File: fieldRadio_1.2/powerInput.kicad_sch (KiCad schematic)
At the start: 7 parts, among them Q21 IRF9540, U10 LM1086-5.0

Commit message: Working on fieldRadio_1.2 schematics
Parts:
- added C230, C231: 4.7uF, PCM_JLCPCB:C_0805, symbol PCM_JLCPCB-Capacitors:0805,4.7uF
- added C232, C233: 100nF, PCM_JLCPCB:C_0603, symbol PCM_JLCPCB-Capacitors:0603,100nF
- added C234, C235: 22uF, PCM_JLCPCB:C_0805, symbol PCM_JLCPCB-Capacitors:0805,22uF
- added C236: 100uF, Capacitor_SMD:C_Elec_6.3x5.8, symbol Device:C_Small_US
- added J13, J9: Conn_01x03, Connector_Wire:SolderWire-0.75sqmm_1x03_P4.8mm_D1.25mm_OD2.3mm, symbol Connector_Generic:Conn_01x03
- added L22: 6.8uH, Inductor_SMD:L_TechFuse_SL0624, symbol Device:L
- added R208: 10kΩ, PCM_JLCPCB:R_0603, symbol PCM_JLCPCB-Resistors:0603,10kΩ
- added R214: 14kΩ, PCM_JLCPCB:R_0603, symbol PCM_JLCPCB-Resistors:0603,30kΩ
- added R220: 100k, PCM_JLCPCB:R_0603, symbol PCM_JLCPCB-Resistors:0603,10kΩ
- added U29: LMR51430, Package_TO_SOT_SMD:SOT-23-6, symbol Regulator_Switching:LMR51430
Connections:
- net +5V: now also J9.2 (Pin_2); no longer C155.1, C156.1, U10.2 (VO)
- net GND: now also C230.2, C231.2, C232.2, C234.2, C235.2, C236.2, R208.2, R214.2, U29.1 (GND)
- net VDD12: now also J13.2 (Pin_2); no longer C153.1, C154.1, U10.3 (VI)
- net at Q21.2 (D): no longer F1.2
- new net: C230.1, C231.1, C232.1, J13.1 (Pin_1), R208.1, U29.3 (VIN), U29.5 (EN)
- new net: C153.1, C154.1, J13.3 (Pin_3), U10.3 (VI)
- new net: C233.1, U29.6 (CB)
- new net +5V_Linear: C155.1, C156.1, J9.3 (Pin_3), U10.2 (VO)
- new net +5V_SWITCHING: C234.1, C235.1, C236.1, J9.1 (Pin_1), L22.2, R220.2
- new net fb2: R214.1, R220.1, U29.4 (FB)
- new net sw2: C233.2, L22.1, U29.2 (SW)
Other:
- moved on the sheet: F1, Q21

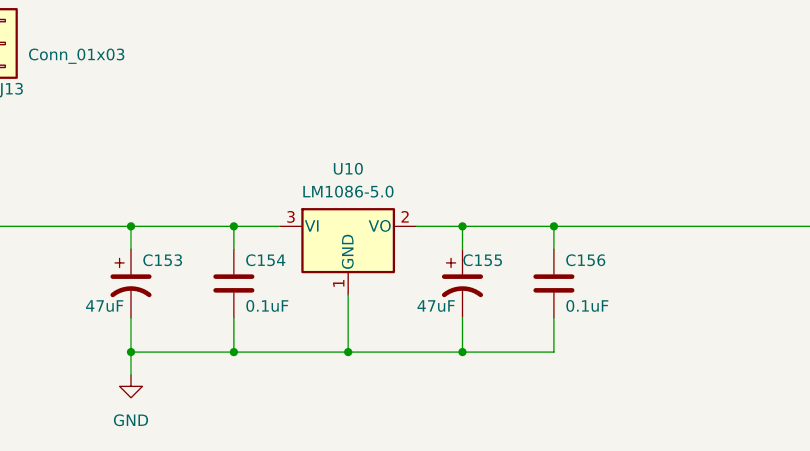
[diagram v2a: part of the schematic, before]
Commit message: adding jlcpcb part numbers to schematics
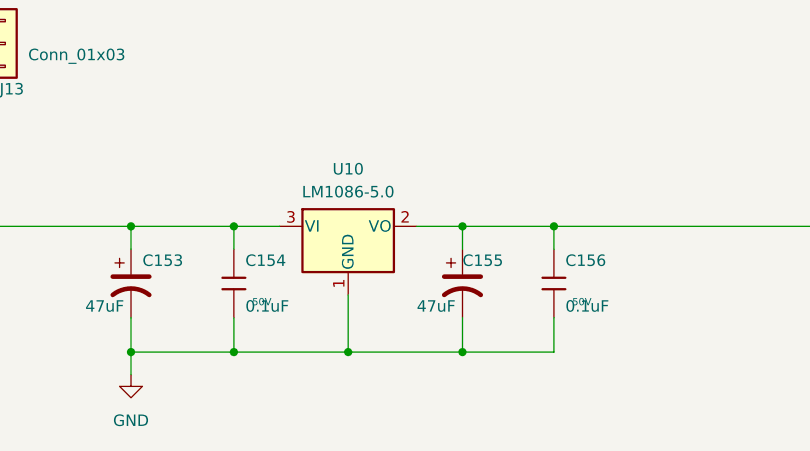
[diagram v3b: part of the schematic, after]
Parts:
- C154, C156: footprint Capacitor_SMD:C_0603_1608Metric_Pad1.08x0.95mm_HandSolder -> PCM_JLCPCB:C_0603; symbol Device:C -> PCM_JLCPCB-Capacitors:0603,100nF; Attrition Qty (none) -> 10; Capacitance (none) -> 100nF; Category (none) -> Capacitors,Multilayer Ceramic Capacitors MLCC - SMD/SMT; Class (none) -> Basic Component; LCSC (none) -> C14663; Manufacturer (none) -> YAGEO; Minimum Qty (none) -> 20; Part (none) -> CC0603KRX7R9BB104; Price (none) -> 0.006USD; Process (none) -> SMT; Stock (none) -> 70324515; Temperature Coefficient (none) -> X7R; Tolerance (none) -> ±10%; Voltage Rated (none) -> 50V
- R220: symbol PCM_JLCPCB-Resistors:0603,10kΩ -> PCM_JLCPCB-Resistors:0603,100kΩ; LCSC C25804 -> C25803; Part 0603WAF1002T5E -> 0603WAF1003T5E; Resistance 10kΩ -> 100kΩ; Stock 51181774 -> 7820113

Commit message: more jlcpcb part number work
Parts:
- F1: JLCPCB (none) -> C139284
- Q21: JLCPCB (none) -> C2575; now left out of the parts list
- U10: JLCPCB (none) -> C16807
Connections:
- net at Q21.2 (D): now also F1.2
- net fb2: no longer names the net of R214.1, R220.1, U29.4 (FB)
- net sw2: no longer names the net of C233.2, L22.1, U29.2 (SW)
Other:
- moved on the sheet: F1
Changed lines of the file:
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@@
 	(wire
 		(pts
-			(xy 97.028 125.73) (xy 107.95 125.73)
-		)
-		(stroke
-			(width 0)
-			(type default)
-		)
-	)
-	(wire
-		(pts
 			(xy 223.52 110.49) (xy 232.41 110.49)
 		)
@@
 	(wire
 		(pts
-			(xy 86.36 125.73) (xy 89.154 125.73)
+			(xy 86.36 125.73) (xy 90.17 125.73)
+		)
+		(stroke
+			(width 0)
+			(type default)
+		)
+	)
+	(wire
+		(pts
+			(xy 97.79 125.73) (xy 107.95 125.73)
 		)
 		(stroke
@@
 		)
 	)
-	(label "sw2"
-		(at 267.97 92.71 0)
-		(effects
-			(font
-				(size 1.27 1.27)
-			)
-			(justify left bottom)
-		)
-	)
 	(label "+5V_SWITCHING"
 		(at 317.5 92.71 0)
@@
 		)
 	)
-	(label "fb2"
-		(at 273.05 95.25 0)
-		(effects
-			(font
-				(size 1.27 1.27)
-			)
-			(justify left bottom)
-		)
-	)
 	(global_label "VDD12"
 		(shape input)
@@
 			)
 		)
+		(property "Mouser Part Number" ""
+			(at 232.41 139.7 0)
+			(hide yes)
+			(show_name no)
+			(do_not_autoplace no)
+			(effects
+				(font
+					(size 1.27 1.27)
+				)
+			)
+		)
+		(property "JLCPCB" "C16807"
+			(at 232.41 139.7 0)
+			(hide yes)
+			(show_name no)
+			(do_not_autoplace no)
+			(effects
+				(font
+					(size 1.27 1.27)
+				)
+			)
+		)
 		(pin "1"
 		)
@@
 		(body_style 1)
 		(exclude_from_sim no)
-		(in_bom yes)
+		(in_bom no)
 		(on_board yes)
 		(in_pos_files yes)
@@
 			)
 		)
+		(property "Mouser Part Number" ""
+			(at 113.03 128.27 0)
+			(hide yes)
+			(show_name no)
+			(do_not_autoplace no)
+			(effects
+				(font
+					(size 1.27 1.27)
+				)
+			)
+		)
+		(property "JLCPCB" "C2575"
+			(at 113.03 128.27 90)
+			(hide yes)
+			(show_name no)
+			(do_not_autoplace no)
+			(effects
+				(font
+					(size 1.27 1.27)
+				)
+			)
+		)
 		(pin "1"
 		)
@@
 	(symbol
 		(lib_id "Device:Fuse")
-		(at 92.964 125.73 90)
+		(at 93.98 125.73 90)
 		(unit 1)
 		(body_style 1)
@@
 		(fields_autoplaced yes)
 		(property "Reference" "F1"
-			(at 92.964 119.38 90)
+			(at 93.98 119.38 90)
 			(show_name no)
 			(do_not_autoplace no)
@@
 		)
 		(property "Value" "Polyfuse"
-			(at 92.964 121.92 90)
+			(at 93.98 121.92 90)
 			(show_name no)
 			(do_not_autoplace no)
@@
 		)
 		(property "Footprint" "Fuse:Fuse_2920_7451Metric_Pad2.10x5.45mm_HandSolder"
-			(at 92.964 127.508 90)
+			(at 93.98 127.508 90)
 			(hide yes)
 			(show_name no)
@@
 		)
 		(property "Datasheet" ""
-			(at 92.964 125.73 0)
+			(at 93.98 125.73 0)
 			(hide yes)
 			(show_name no)
@@
 		)
 		(property "Description" ""
-			(at 92.964 125.73 0)
+			(at 93.98 125.73 0)
+			(show_name no)
+			(do_not_autoplace no)
+			(effects
+				(font
+					(size 1.27 1.27)
+				)
+			)
+		)
+		(property "Mouser Part Number" ""
+			(at 93.98 125.73 0)
+			(hide yes)
+			(show_name no)
+			(do_not_autoplace no)
+			(effects
+				(font
+					(size 1.27 1.27)
+				)
+			)
+		)
+		(property "JLCPCB" "C139284"
+			(at 93.98 125.73 90)
+			(hide yes)
 			(show_name no)
 			(do_not_autoplace no)

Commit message: continued symbol property updates
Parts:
- removed C153, C155: 47uF, Capacitor_THT:CP_Radial_D7.5mm_P2.50mm, symbol Device:C_Polarized_US
- removed R214: 14kΩ, PCM_JLCPCB:R_0603, symbol PCM_JLCPCB-Resistors:0603,30kΩ
- added C54, C55: 47uF, Capacitor_SMD:CP_Elec_6.3x5.8, symbol Device:C_Polarized_US
- added R224: 12kΩ, PCM_JLCPCB:R_0603, symbol PCM_JLCPCB-Resistors:0603,12kΩ
- added R225: 2kΩ, PCM_JLCPCB:R_0603, symbol PCM_JLCPCB-Resistors:0603,2kΩ
- F1: LCSC (none) -> C139284
- J13, J9: now left out of the parts list
- L22: LCSC (none) -> C22463814
- Q21: LCSC (none) -> C2575
- U10: LCSC (none) -> C16807; now left out of the parts list
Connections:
- net +5V_Linear: now also C55.1
- net GND: now also C54.2, C55.2, R225.2
- net at C154.1, J13.3 (Pin_3), U10.3 (VI): now also C54.1
- net at R220.1, U29.4 (FB): now also R224.2
- new net: R224.1, R225.1

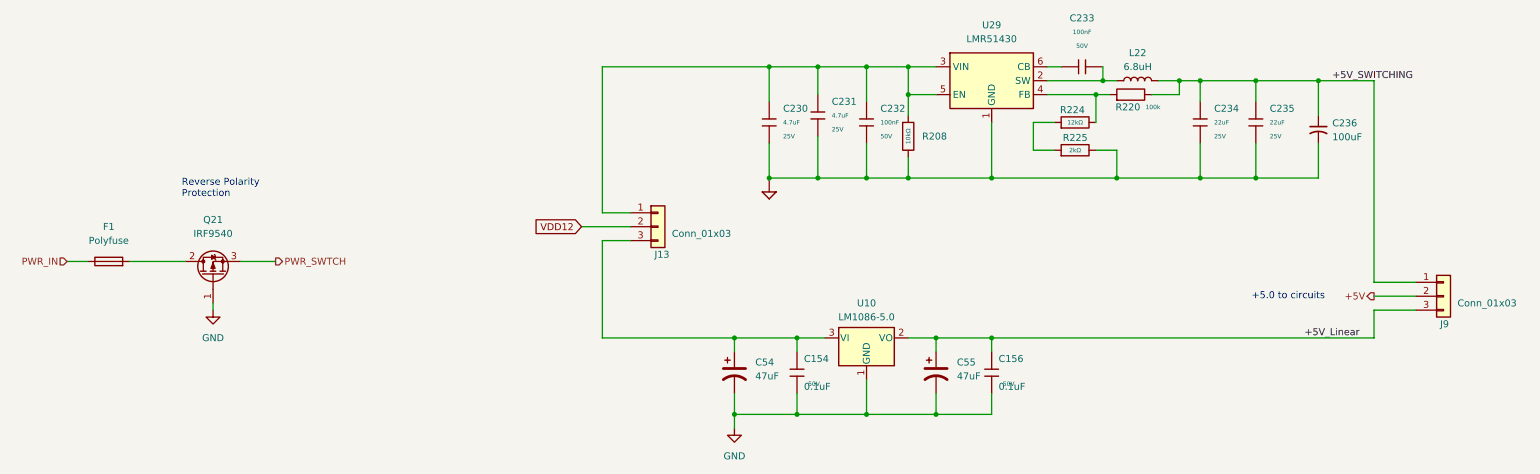
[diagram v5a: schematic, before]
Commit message: Starting fieldRadio1.2 layout
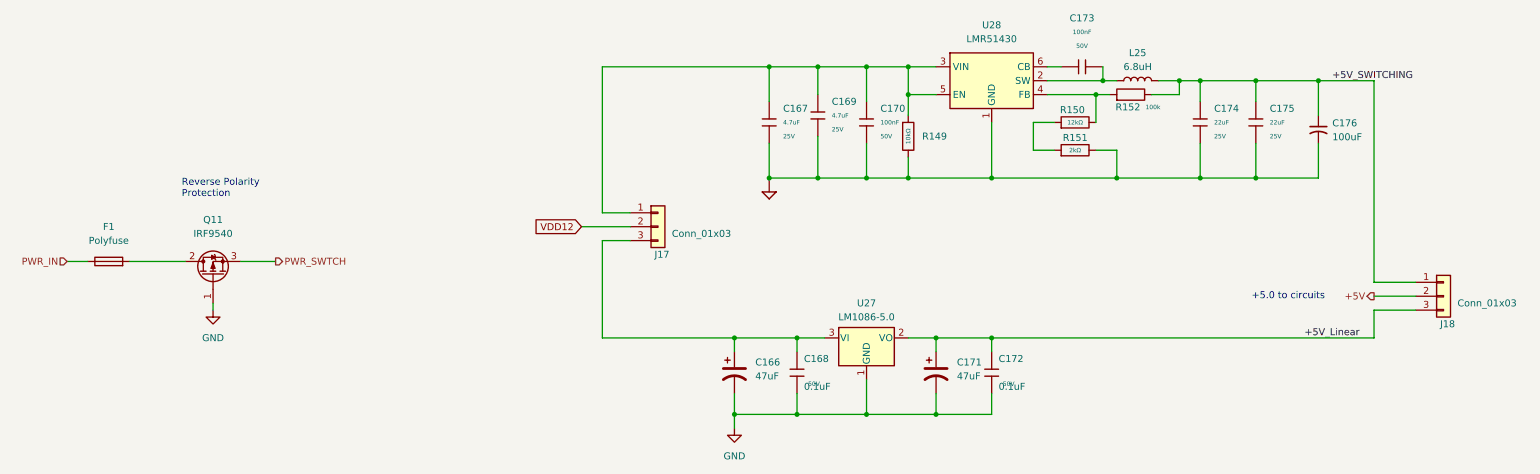
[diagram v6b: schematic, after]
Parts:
- renumbered C54 to C166, C230 to C167, C154 to C168, C231 to C169, C232 to C170, C55 to C171, C156 to C172, C233 to C173, C234 to C174, C235 to C175, C236 to C176, J13 to J17, J9 to J18, L22 to L25, Q21 to Q11, R208 to R149, R224 to R150, R225 to R151, R220 to R152, U10 to U27, U29 to U28
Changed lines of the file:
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@@
 		(in_pos_files yes)
 		(dnp no)
-		(property "Reference" "J13"
+		(property "Reference" "J17"
 			(at 193.675 124.46 0)
 			(show_name no)
@@
 			(project "fieldRadio_1.2"
 				(path "/a1d1b2b0-2f27-4dc0-94ba-bb0e02933617/56bfcbb6-5b4c-41a3-a0f1-0c3e063460f4"
-					(reference "J13")
+					(reference "J17")
 					(unit 1)
 				)
@@
 		(dnp no)
 		(fields_autoplaced yes)
-		(property "Reference" "C55"
+		(property "Reference" "C171"
 			(at 248.92 144.1449 0)
 			(show_name no)
@@
 			(project "fieldRadio_1.2"
 				(path "/a1d1b2b0-2f27-4dc0-94ba-bb0e02933617/56bfcbb6-5b4c-41a3-a0f1-0c3e063460f4"
-					(reference "C55")
+					(reference "C171")
 					(unit 1)
 				)
@@
 		(in_pos_files yes)
 		(dnp no)
-		(property "Reference" "#SUPPLY042"
+		(property "Reference" "#SUPPLY030"
 			(at 214.63 113.03 0)
 			(hide yes)
@@
 			(project "fieldRadio_1.2"
 				(path "/a1d1b2b0-2f27-4dc0-94ba-bb0e02933617/56bfcbb6-5b4c-41a3-a0f1-0c3e063460f4"
-					(reference "#SUPPLY042")
+					(reference "#SUPPLY030")
 					(unit 1)
 				)
@@
 		(dnp no)
 		(fields_autoplaced yes)
-		(property "Reference" "C54"
+		(property "Reference" "C166"
 			(at 212.09 144.1449 0)
 			(show_name no)
@@
 			(project "fieldRadio_1.2"
 				(path "/a1d1b2b0-2f27-4dc0-94ba-bb0e02933617/56bfcbb6-5b4c-41a3-a0f1-0c3e063460f4"
-					(reference "C54")
+					(reference "C166")
 					(unit 1)
 				)
@@
 		(in_pos_files yes)
 		(dnp no)
-		(property "Reference" "C154"
+		(property "Reference" "C168"
 			(at 220.98 143.51 0)
 			(show_name no)
@@
 			(project "fieldRadio_1.2"
 				(path "/a1d1b2b0-2f27-4dc0-94ba-bb0e02933617/56bfcbb6-5b4c-41a3-a0f1-0c3e063460f4"
-					(reference "C154")
+					(reference "C168")
 					(unit 1)
 				)
@@
 		(in_pos_files yes)
 		(dnp no)
-		(property "Reference" "R225"
+		(property "Reference" "R151"
 			(at 272.796 103.124 90)
 			(show_name no)
@@
 			(project "fieldRadio_1.2"
 				(path "/a1d1b2b0-2f27-4dc0-94ba-bb0e02933617/56bfcbb6-5b4c-41a3-a0f1-0c3e063460f4"
-					(reference "R225")
+					(reference "R151")
 					(unit 1)
 				)
@@
 		(dnp no)
 		(fields_autoplaced yes)
-		(property "Reference" "C231"
+		(property "Reference" "C169"
 			(at 226.06 96.5199 0)
 			(show_name no)
@@
 			(project "fieldRadio_1.2"
 				(path "/a1d1b2b0-2f27-4dc0-94ba-bb0e02933617/56bfcbb6-5b4c-41a3-a0f1-0c3e063460f4"
-					(reference "C231")
+					(reference "C169")
 					(unit 1)
 				)
@@
 		(in_pos_files yes)
 		(dnp no)
-		(property "Reference" "R220"
+		(property "Reference" "R152"
 			(at 280.162 97.536 90)
 			(show_name no)
@@
 			(project "fieldRadio_1.2"
 				(path "/a1d1b2b0-2f27-4dc0-94ba-bb0e02933617/56bfcbb6-5b4c-41a3-a0f1-0c3e063460f4"
-					(reference "R220")
+					(reference "R152")
 					(unit 1)
 				)
@@
 		(dnp no)
 		(fields_autoplaced yes)
-		(property "Reference" "U10"
+		(property "Reference" "U27"
 			(at 232.41 133.35 0)
 			(show_name no)
@@
 			(project "fieldRadio_1.2"
 				(path "/a1d1b2b0-2f27-4dc0-94ba-bb0e02933617/56bfcbb6-5b4c-41a3-a0f1-0c3e063460f4"
-					(reference "U10")
+					(reference "U27")
 					(unit 1)
 				)
@@
 		(dnp no)
 		(fields_autoplaced yes)
-		(property "Reference" "C233"
+		(property "Reference" "C173"
 			(at 271.78 81.28 90)
 			(show_name no)
@@
 			(project "fieldRadio_1.2"
 				(path "/a1d1b2b0-2f27-4dc0-94ba-bb0e02933617/56bfcbb6-5b4c-41a3-a0f1-0c3e063460f4"
-					(reference "C233")
+					(reference "C173")
 					(unit 1)
 				)
@@
 		(dnp no)
 		(fields_autoplaced yes)
-		(property "Reference" "Q21"
+		(property "Reference" "Q11"
 			(at 113.03 118.11 90)
 			(show_name no)
@@
 			(project "fieldRadio_1.2"
 				(path "/a1d1b2b0-2f27-4dc0-94ba-bb0e02933617/56bfcbb6-5b4c-41a3-a0f1-0c3e063460f4"
-					(reference "Q21")
+					(reference "Q11")
 					(unit 1)
 				)
@@
 		(dnp no)
 		(fields_autoplaced yes)
-		(property "Reference" "C232"
+		(property "Reference" "C170"
 			(at 234.95 97.7899 0)
 			(show_name no)
@@
 			(project "fieldRadio_1.2"
 				(path "/a1d1b2b0-2f27-4dc0-94ba-bb0e02933617/56bfcbb6-5b4c-41a3-a0f1-0c3e063460f4"
-					(reference "C232")
+					(reference "C170")
 					(unit 1)
 				)
@@
 		(dnp no)
 		(fields_autoplaced yes)
-		(property "Reference" "C236"
+		(property "Reference" "C176"
 			(at 317.5 100.4569 0)
 			(show_name no)
@@
 			(project "fieldRadio_1.2"
 				(path "/a1d1b2b0-2f27-4dc0-94ba-bb0e02933617/56bfcbb6-5b4c-41a3-a0f1-0c3e063460f4"
-					(reference "C236")
+					(reference "C176")
 					(unit 1)
 				)
@@
 		(dnp no)
 		(fields_autoplaced yes)
-		(property "Reference" "#PWR029"
+		(property "Reference" "#PWR052"
 			(at 113.03 140.97 0)
 			(hide yes)
@@
 			(project "fieldRadio_1.2"
 				(path "/a1d1b2b0-2f27-4dc0-94ba-bb0e02933617/56bfcbb6-5b4c-41a3-a0f1-0c3e063460f4"
-					(reference "#PWR029")
+					(reference "#PWR052")
 					(unit 1)
 				)
@@
 		(in_pos_files yes)
 		(dnp no)
-		(property "Reference" "C156"
+		(property "Reference" "C172"
 			(at 256.54 143.51 0)
 			(show_name no)
@@
 			(project "fieldRadio_1.2"
 				(path "/a1d1b2b0-2f27-4dc0-94ba-bb0e02933617/56bfcbb6-5b4c-41a3-a0f1-0c3e063460f4"
-					(reference "C156")
+					(reference "C172")
 					(unit 1)
 				)
@@
 		(in_pos_files yes)
 		(dnp no)
-		(property "Reference" "R224"
+		(property "Reference" "R150"
 			(at 272.288 98.044 90)
 			(show_name no)
@@
 			(project "fieldRadio_1.2"
 				(path "/a1d1b2b0-2f27-4dc0-94ba-bb0e02933617/56bfcbb6-5b4c-41a3-a0f1-0c3e063460f4"
-					(reference "R224")
+					(reference "R150")
 					(unit 1)
 				)
@@
 		(dnp no)
 		(fields_autoplaced yes)
-		(property "Reference" "R208"
+		(property "Reference" "R149"
 			(at 242.57 102.8699 0)
 			(show_name no)
@@
 			(project "fieldRadio_1.2"
 				(path "/a1d1b2b0-2f27-4dc0-94ba-bb0e02933617/56bfcbb6-5b4c-41a3-a0f1-0c3e063460f4"
-					(reference "R208")
+					(reference "R149")
 					(unit 1)
 				)
@@
 		(dnp no)
 		(fields_autoplaced yes)
-		(property "Reference" "U29"
+		(property "Reference" "U28"
 			(at 255.27 82.55 0)
 			(show_name no)
@@
 			(project "fieldRadio_1.2"
 				(path "/a1d1b2b0-2f27-4dc0-94ba-bb0e02933617/56bfcbb6-5b4c-41a3-a0f1-0c3e063460f4"
-					(reference "U29")
+					(reference "U28")
 					(unit 1)
 				)
@@
 		(dnp no)
 		(fields_autoplaced yes)
-		(property "Reference" "C230"
+		(property "Reference" "C167"
 			(at 217.17 97.7899 0)
 			(show_name no)
@@
 			(project "fieldRadio_1.2"
 				(path "/a1d1b2b0-2f27-4dc0-94ba-bb0e02933617/56bfcbb6-5b4c-41a3-a0f1-0c3e063460f4"
-					(reference "C230")
+					(reference "C167")
 					(unit 1)
 				)
@@
 		(dnp no)
 		(fields_autoplaced yes)
-		(property "Reference" "C235"
+		(property "Reference" "C175"
 			(at 306.07 97.7899 0)
 			(show_name no)
@@
 			(project "fieldRadio_1.2"
 				(path "/a1d1b2b0-2f27-4dc0-94ba-bb0e02933617/56bfcbb6-5b4c-41a3-a0f1-0c3e063460f4"
-					(reference "C235")
+					(reference "C175")
 					(unit 1)
 				)
@@
 		(dnp no)
 		(fields_autoplaced yes)
-		(property "Reference" "L22"
+		(property "Reference" "L25"
 			(at 281.94 87.63 90)
 			(show_name no)
@@
 			(project "fieldRadio_1.2"
 				(path "/a1d1b2b0-2f27-4dc0-94ba-bb0e02933617/56bfcbb6-5b4c-41a3-a0f1-0c3e063460f4"
-					(reference "L22")
+					(reference "L25")
 					(unit 1)
 				)
@@
 		(dnp no)
 		(fields_autoplaced yes)
-		(property "Reference" "C234"
+		(property "Reference" "C174"
 			(at 295.91 97.7899 0)
 			(show_name no)
@@
 			(project "fieldRadio_1.2"
 				(path "/a1d1b2b0-2f27-4dc0-94ba-bb0e02933617/56bfcbb6-5b4c-41a3-a0f1-0c3e063460f4"
-					(reference "C234")
+					(reference "C174")
 					(unit 1)
 				)
@@
 		(dnp no)
 		(fields_autoplaced yes)
-		(property "Reference" "#PWR039"
+		(property "Reference" "#PWR053"
 			(at 208.28 162.56 0)
 			(hide yes)
@@
 			(project "fieldRadio_1.2"
 				(path "/a1d1b2b0-2f27-4dc0-94ba-bb0e02933617/56bfcbb6-5b4c-41a3-a0f1-0c3e063460f4"
-					(reference "#PWR039")
+					(reference "#PWR053")
 					(unit 1)
 				)
@@
 		(in_pos_files yes)
 		(dnp no)
-		(property "Reference" "J9"
+		(property "Reference" "J18"
 			(at 337.185 137.16 0)
 			(show_name no)
@@
 			(project "fieldRadio_1.2"
 				(path "/a1d1b2b0-2f27-4dc0-94ba-bb0e02933617/56bfcbb6-5b4c-41a3-a0f1-0c3e063460f4"
-					(reference "J9")
+					(reference "J18")
 					(unit 1)
 				)

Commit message: continued placement work
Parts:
- removed C167, C169: 4.7uF, PCM_JLCPCB:C_0805, symbol PCM_JLCPCB-Capacitors:0805,4.7uF
- removed C170, C173: 100nF, PCM_JLCPCB:C_0603, symbol PCM_JLCPCB-Capacitors:0603,100nF
- removed C174, C175: 22uF, PCM_JLCPCB:C_0805, symbol PCM_JLCPCB-Capacitors:0805,22uF
- removed C176: 100uF, Capacitor_SMD:C_Elec_6.3x5.8, symbol Device:C_Small_US
- removed J17, J18: Conn_01x03, Connector_Wire:SolderWire-0.75sqmm_1x03_P4.8mm_D1.25mm_OD2.3mm, symbol Connector_Generic:Conn_01x03
- removed L25: 6.8uH, Inductor_SMD:L_TechFuse_SL0624, symbol Device:L
- removed R149: 10kΩ, PCM_JLCPCB:R_0603, symbol PCM_JLCPCB-Resistors:0603,10kΩ
- removed R150: 12kΩ, PCM_JLCPCB:R_0603, symbol PCM_JLCPCB-Resistors:0603,12kΩ
- removed R151: 2kΩ, PCM_JLCPCB:R_0603, symbol PCM_JLCPCB-Resistors:0603,2kΩ
- removed R152: 100k, PCM_JLCPCB:R_0603, symbol PCM_JLCPCB-Resistors:0603,100kΩ
- removed U28: LMR51430, Package_TO_SOT_SMD:SOT-23-6, symbol Regulator_Switching:LMR51430
- U27: value LM1086-5.0 -> L7805ABD2T-TR; footprint Package_TO_SOT_THT:TO-220-3_Vertical -> Package_TO_SOT_SMD:TO-263-2; symbol Regulator_Linear:LM1085-5.0 -> Regulator_Linear:L7805; JLCPCB C16807 -> C86206; LCSC C16807 -> C86206; now in the parts list
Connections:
- net +5V: now also C171.1, C172.1, U27.3 (OUT)
- net GND: now also U27.2 (GND); no longer U27.1 (GND)
- net VDD12: now also C166.1, C168.1, U27.1 (IN)
- removed net +5V_Linear: C171.1, C172.1, U27.2 (VO)
